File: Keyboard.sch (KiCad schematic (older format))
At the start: 56 parts, among them SW1 SW_Push, U1 ATmega32U4-AU, Y1 16MHz

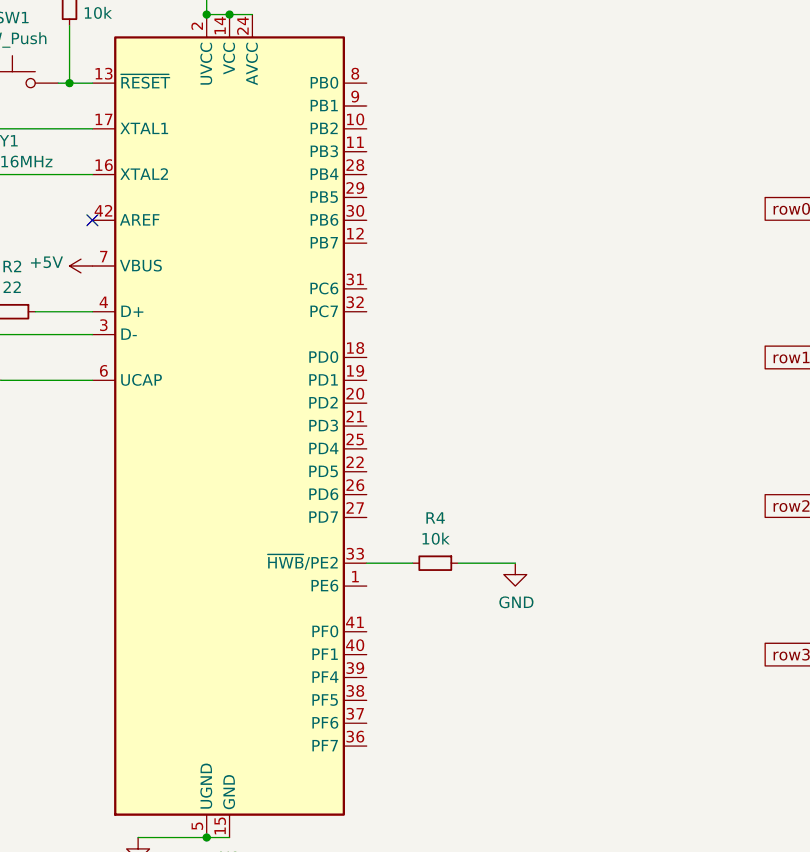
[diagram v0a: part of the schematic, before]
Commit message: terribly connected key matrix
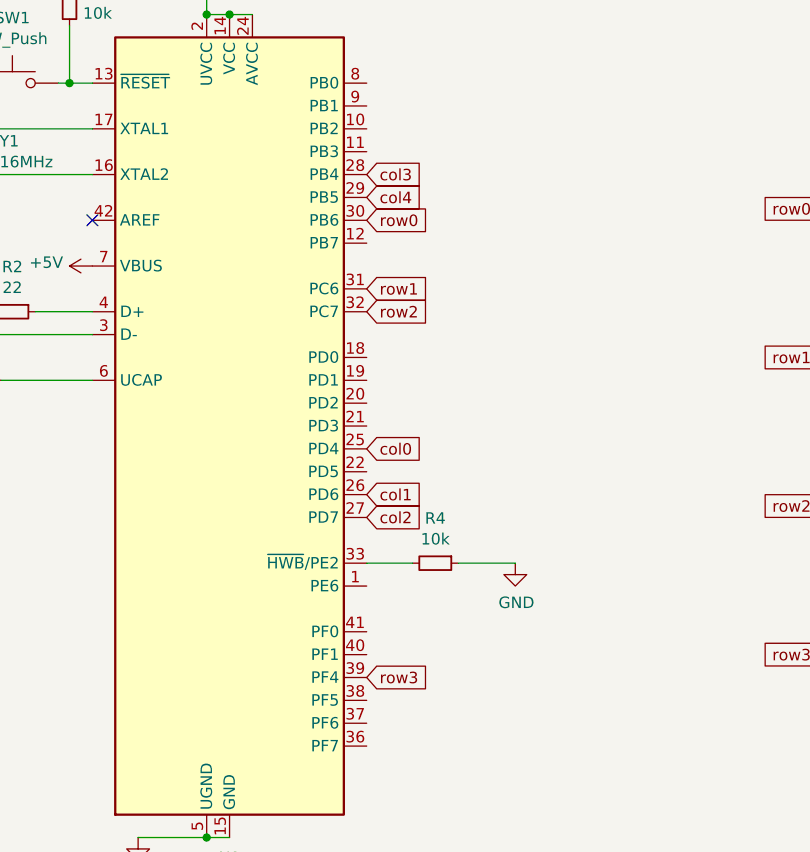
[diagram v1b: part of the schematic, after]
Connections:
- net col0: now also U1.25 (PD4)
- net col1: now also U1.26 (PD6)
- net col2: now also U1.27 (PD7)
- net col3: now also U1.28 (PB4)
- net col4: now also U1.29 (PB5)
- net row0: now also U1.30 (PB6)
- net row1: now also U1.31 (PC6)
- net row2: now also U1.32 (PC7)
- net row3: now also U1.39 (PF4)
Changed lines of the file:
@@
 col4
 NoConn ~ 2150 2450
+Text GLabel 3350 3450 2    50   Input ~ 0
+col0
+Text GLabel 3350 3650 2    50   Input ~ 0
+col1
+Text GLabel 3350 3750 2    50   Input ~ 0
+col2
+Text GLabel 3350 2250 2    50   Input ~ 0
+col3
+Text GLabel 3350 2350 2    50   Input ~ 0
+col4
+Text GLabel 3350 2450 2    50   Input ~ 0
+row0
+Text GLabel 3350 2750 2    50   Input ~ 0
+row1
+Text GLabel 3350 2850 2    50   Input ~ 0
+row2
+Text GLabel 3350 4450 2    50   Input ~ 0
+row3
 $EndSCHEMATC
